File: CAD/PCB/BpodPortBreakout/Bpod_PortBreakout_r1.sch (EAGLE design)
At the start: 9 parts

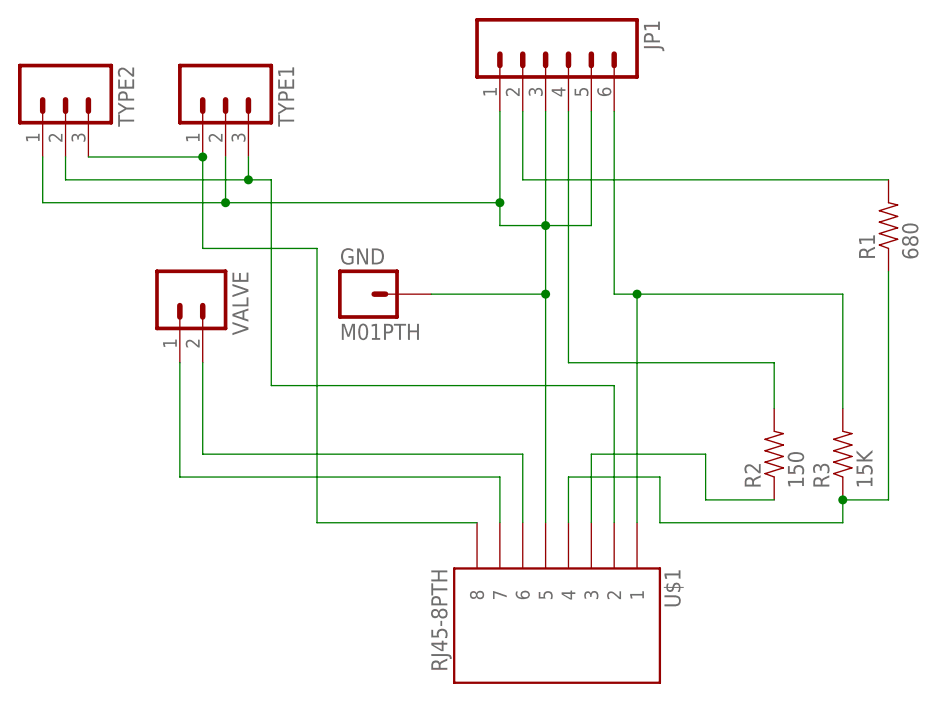
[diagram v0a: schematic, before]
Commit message: Major update: -Integrates with PsychToolbox (if installed) for low latency serial and possible future use as a sound server -Adds sound support with Teensy Audio board, added as a hardware serial device -Updated to work on Ubuntu 14 with MATLAB r2011a or newer (must create a serial port alias: /dev/TTYACM0 --> /dev/TTYS101) -Added hardware serial override to GUI -Many other bug-fixes
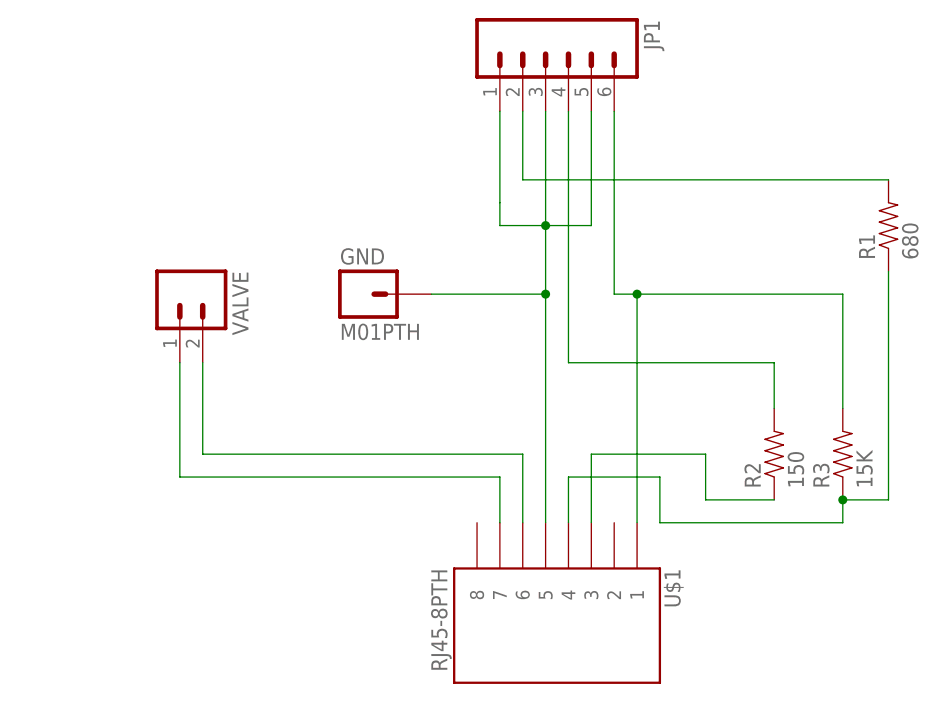
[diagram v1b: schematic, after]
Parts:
- removed TYPE1, TYPE2: (no value), SparkFun:M03PTH
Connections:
- removed net N$11: TYPE1.1, TYPE2.3, U$1.8
- removed net N$9: TYPE1.3, TYPE2.2, U$1.2
- net N$4: no longer TYPE1.2, TYPE2.1
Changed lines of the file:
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@@
 <part name="VALVE" library="SparkFun" deviceset="M02" device="3.5MM_LOCK"/>
 <part name="GND" library="SparkFun" deviceset="M01" device="PTH"/>
-<part name="TYPE1" library="SparkFun" deviceset="M03" device="PTH"/>
-<part name="TYPE2" library="SparkFun" deviceset="M03" device="PTH"/>
 </parts>
 <sheets>
@@
 <attribute name="VALUE" x="58.42" y="33.02" size="1.778" layer="96"/>
 </instance>
-<instance part="TYPE1" gate="G$1" x="45.72" y="60.96" rot="R270"/>
-<instance part="TYPE2" gate="G$1" x="27.94" y="60.96" rot="R270"/>
 </instances>
 <busses>
@@
 <wire x1="86.36" y1="58.42" x2="86.36" y2="45.72" width="0.1524" layer="91"/>
 <wire x1="68.58" y1="38.1" x2="81.28" y2="38.1" width="0.1524" layer="91"/>
-<wire x1="45.72" y1="53.34" x2="45.72" y2="48.26" width="0.1524" layer="91"/>
-<wire x1="45.72" y1="48.26" x2="76.2" y2="48.26" width="0.1524" layer="91"/>
-<wire x1="25.4" y1="53.34" x2="25.4" y2="48.26" width="0.1524" layer="91"/>
-<wire x1="25.4" y1="48.26" x2="45.72" y2="48.26" width="0.1524" layer="91"/>
 <junction x="81.28" y="45.72"/>
 <junction x="81.28" y="38.1"/>
-<junction x="76.2" y="48.26"/>
-<junction x="45.72" y="48.26"/>
 <pinref part="U$1" gate="G$1" pin="5"/>
 <pinref part="JP1" gate="G$1" pin="1"/>
@@
 <pinref part="JP1" gate="G$1" pin="5"/>
 <pinref part="GND" gate="G$1" pin="1"/>
-<pinref part="TYPE1" gate="G$1" pin="2"/>
-<pinref part="TYPE2" gate="G$1" pin="1"/>
 </segment>
 </net>
@@
 </segment>
 </net>
-<net name="N$9" class="0">
-<segment>
-<wire x1="88.9" y1="12.7" x2="88.9" y2="27.94" width="0.1524" layer="91"/>
-<wire x1="88.9" y1="27.94" x2="50.8" y2="27.94" width="0.1524" layer="91"/>
-<wire x1="50.8" y1="27.94" x2="50.8" y2="50.8" width="0.1524" layer="91"/>
-<wire x1="50.8" y1="50.8" x2="48.26" y2="50.8" width="0.1524" layer="91"/>
-<wire x1="48.26" y1="50.8" x2="48.26" y2="53.34" width="0.1524" layer="91"/>
-<wire x1="27.94" y1="53.34" x2="27.94" y2="50.8" width="0.1524" layer="91"/>
-<wire x1="27.94" y1="50.8" x2="48.26" y2="50.8" width="0.1524" layer="91"/>
-<junction x="48.26" y="50.8"/>
-<pinref part="U$1" gate="G$1" pin="2"/>
-<pinref part="TYPE1" gate="G$1" pin="3"/>
-<pinref part="TYPE2" gate="G$1" pin="2"/>
-</segment>
-</net>
-<net name="N$11" class="0">
-<segment>
-<wire x1="43.18" y1="53.34" x2="43.18" y2="43.18" width="0.1524" layer="91"/>
-<wire x1="43.18" y1="43.18" x2="55.88" y2="43.18" width="0.1524" layer="91"/>
-<wire x1="55.88" y1="43.18" x2="55.88" y2="12.7" width="0.1524" layer="91"/>
-<wire x1="55.88" y1="12.7" x2="73.66" y2="12.7" width="0.1524" layer="91"/>
-<wire x1="30.48" y1="53.34" x2="43.18" y2="53.34" width="0.1524" layer="91"/>
-<junction x="43.18" y="53.34"/>
-<pinref part="TYPE1" gate="G$1" pin="1"/>
-<pinref part="U$1" gate="G$1" pin="8"/>
-<pinref part="TYPE2" gate="G$1" pin="3"/>
-</segment>
-</net>
